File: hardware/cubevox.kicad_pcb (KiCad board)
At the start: 4 copper layers, 200 x 150 mm, 223 parts, among them J1 USB-C, J101 J_IN NCJ6FA-H, J106 DC 9V, J108 OUT 6.35mm, J117 OLED SH1106, J3 TC2030-NL SWD, K101 G6K-2F-Y DC5, K102 G6K-2F-Y DC5, Q101 MMBT3904, SW101 ST-0-102 bat toggle, SW102 ST-0-102 bat toggle, SW103 ST-0-102 bat toggle, SW104 ST-0-102 bat toggle, SW105 ST-0-102 bat toggle, SW106 ST-0-102 bat toggle, SW107 ST-0-102 bat toggle, SW108 ST-0-102 bat toggle, U1 STM32H743VIT6, U101 CD74HC4067, U103 AP63205WU-7, U104 OPA2197IDR, U105 OPA2197IDR, U106 OPA2197IDR, U3 AP63203WU-7, U4 TLV75533PDBVR, U6 PCM5102APWR, U8 PCM1808PWR, Y1 25MHz 12pF

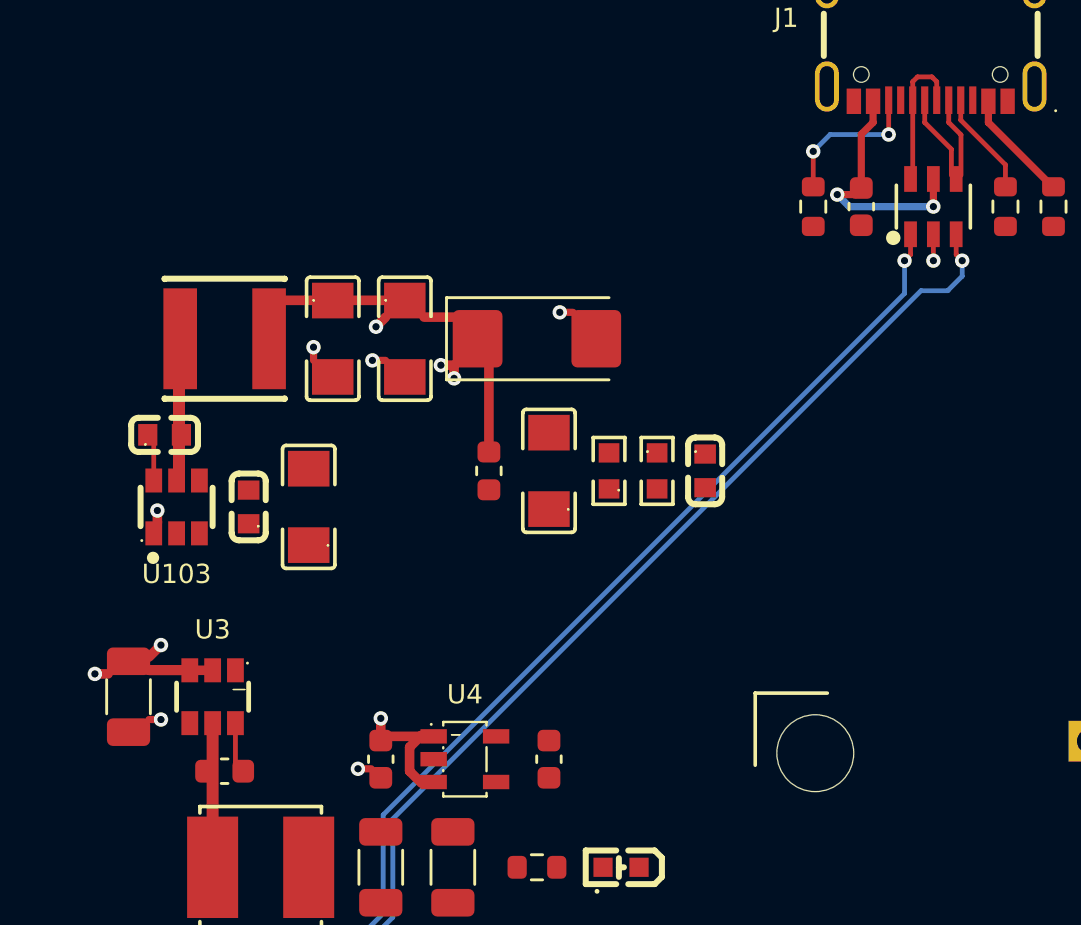
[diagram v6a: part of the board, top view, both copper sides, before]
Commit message: layout: change on /5V,/GND (ledger 0096)
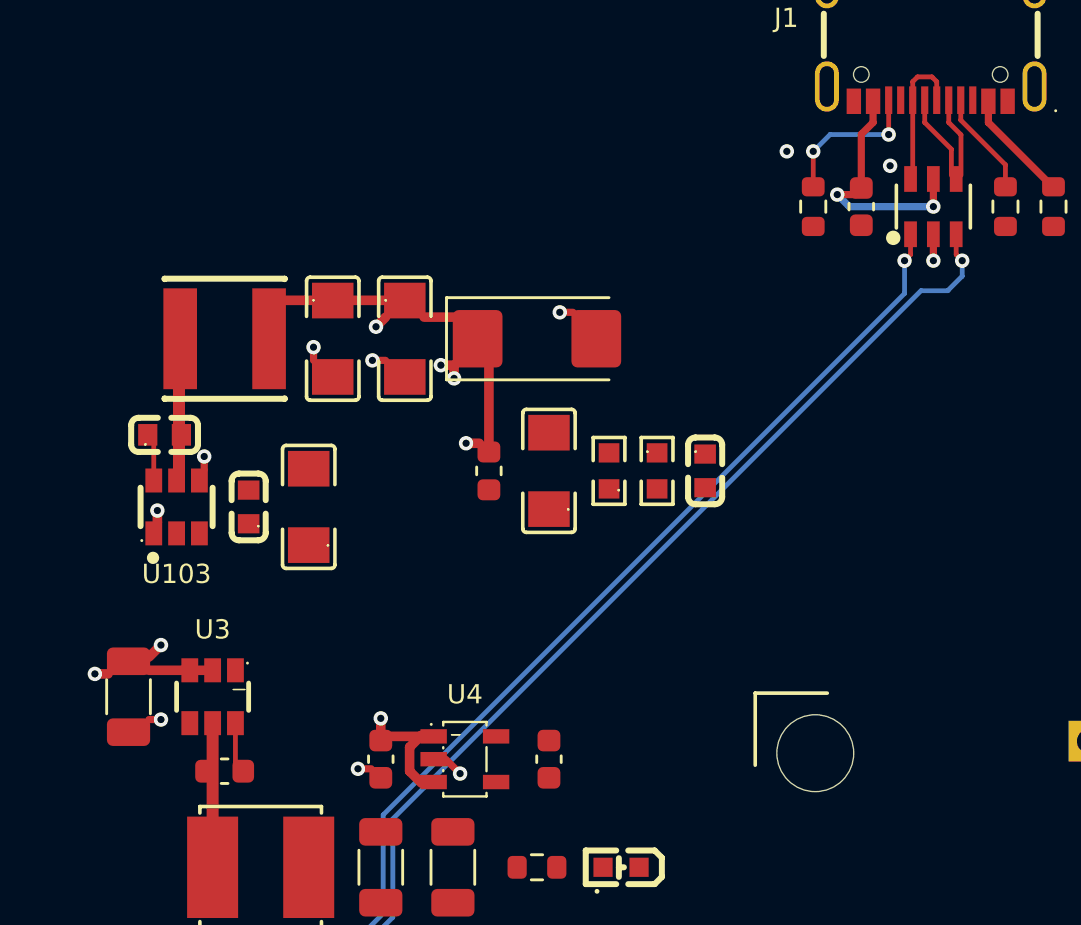
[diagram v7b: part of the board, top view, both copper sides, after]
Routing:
- net /GND: track 3.80 -> 5.20 mm, vias 7 -> 11
- net /5V: track 94.8 -> 94.0 mm, vias 8 -> 9
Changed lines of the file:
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@@
 	)
 	(segment
-		(start 125.5 41.65)
-		(end 125.5 42.75)
-		(width 0.2)
+		(start 105.2 63.5)
+		(end 105.8 64.099999)
+		(width 0.3)
 		(layer "F.Cu")
 		(net "/GND")
@@
 	)
 	(segment
+		(start 125.5 41.65)
+		(end 125.5 42.75)
+		(width 0.3)
+		(layer "F.Cu")
+		(net "/GND")
+	)
+	(segment
+		(start 95.15 51.45)
+		(end 95.15 50.9)
+		(width 0.3)
+		(layer "F.Cu")
+		(net "/GND")
+	)
+	(segment
 		(start 92.85 61.85)
 		(end 93.35 61.85)
@@
 	)
 	(via
+		(at 119.4 38.2)
+		(size 0.6)
+		(drill 0.3)
+		(layers "F.Cu" "B.Cu")
+		(net "/GND")
+	)
+	(via
+		(at 105.8 64.099999)
+		(size 0.6)
+		(drill 0.3)
+		(layers "F.Cu" "B.Cu")
+		(net "/GND")
+	)
+	(via
 		(at 109.95 44.9)
 		(size 0.6)
@@
 	)
 	(via
+		(at 123.7 38.8)
+		(size 0.6)
+		(drill 0.3)
+		(layers "F.Cu" "B.Cu")
+		(net "/GND")
+	)
+	(via
 		(at 101.55 63.9)
 		(size 0.6)
@@
 	(via
 		(at 125.5 42.75)
+		(size 0.6)
+		(drill 0.3)
+		(layers "F.Cu" "B.Cu")
+		(net "/GND")
+	)
+	(via
+		(at 95.15 50.9)
 		(size 0.6)
 		(drill 0.3)
@@
 	)
 	(segment
-		(start 92.85 59.8)
-		(end 95.2 59.8)
-		(width 0.4)
-		(layer "F.Cu")
-		(net "/5V")
-	)
-	(segment
 		(start 104.2 62.5)
 		(end 103.7 63)
@@
 	)
 	(segment
+		(start 94.25 59.8)
+		(end 95.2 59.8)
+		(width 0.4)
+		(layer "F.Cu")
+		(net "/5V")
+	)
+	(segment
 		(start 105.55 47.1)
 		(end 105 47.1)
@@
 	)
 	(segment
+		(start 106.6 50.35)
+		(end 106.05 50.35)
+		(width 0.4)
+		(layer "F.Cu")
+		(net "/5V")
+	)
+	(segment
 		(start 93.35 58.75)
 		(end 92.85 59.25)
@@
 		(size 0.6)
 		(drill 0.3)
+		(layers "F.Cu" "B.Cu")
+		(net "/5V")
+	)
+	(via
+		(at 106.05 50.35)
+		(size 0.6)
+		(drill 0.3)

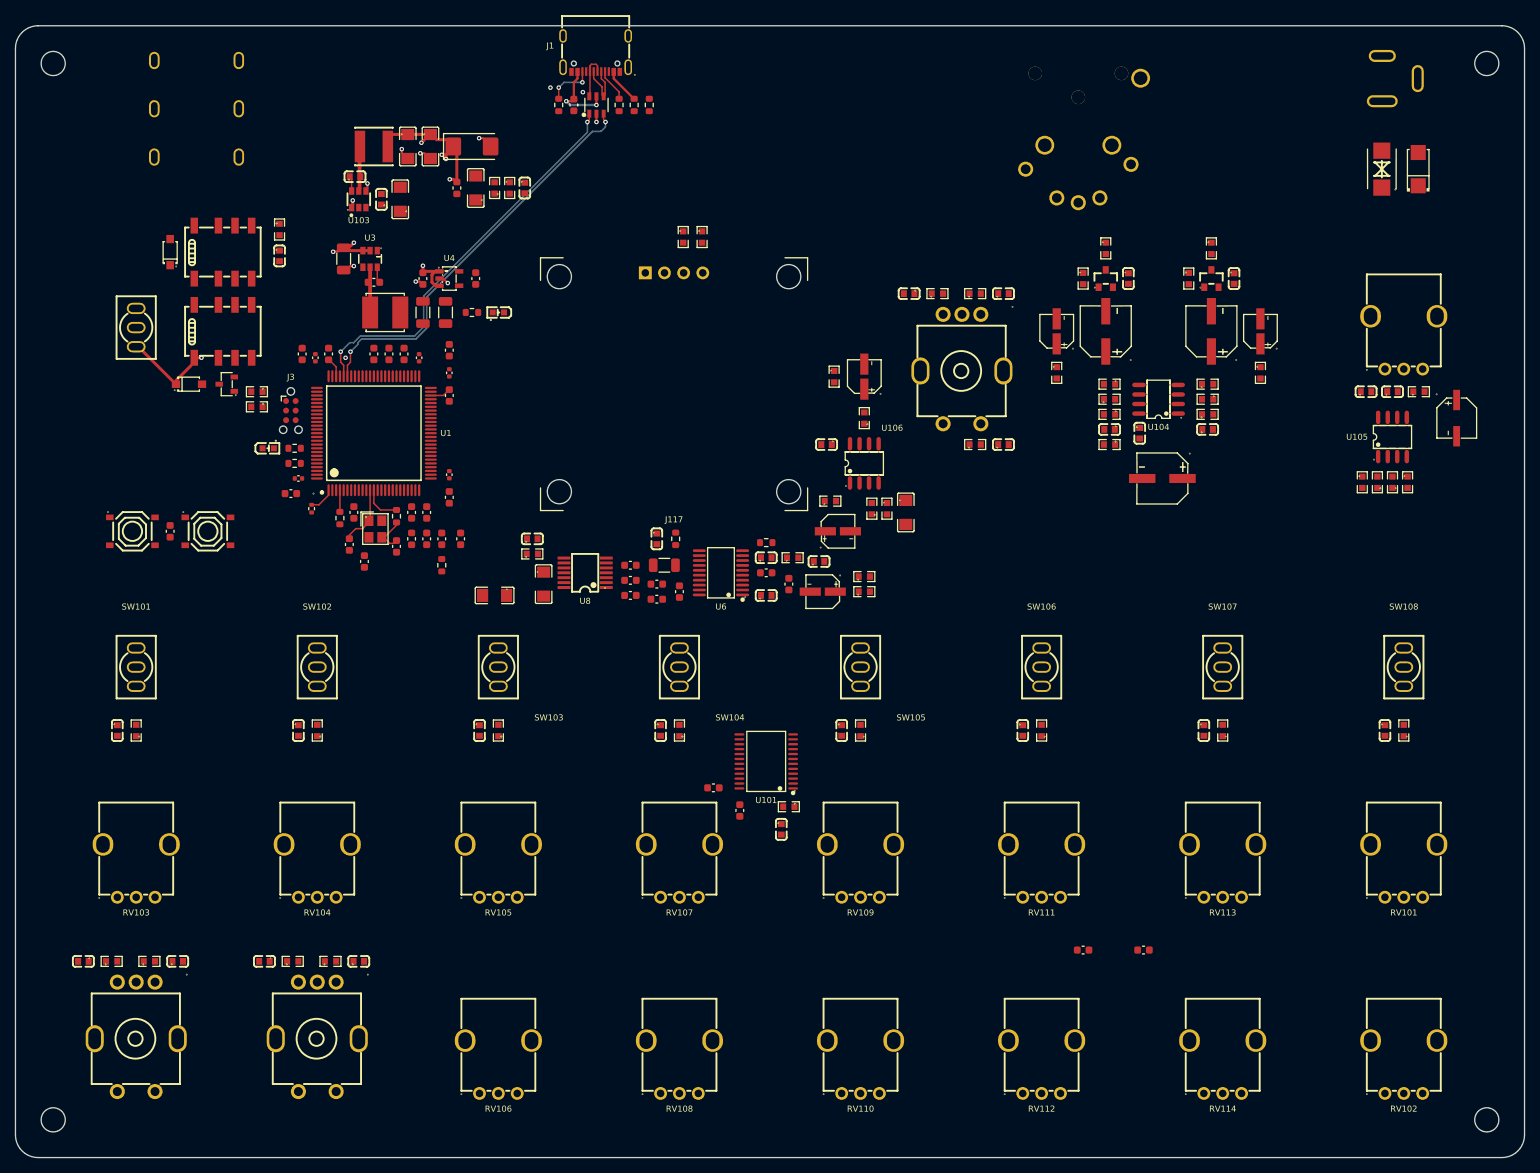
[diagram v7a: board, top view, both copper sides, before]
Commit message: layout: change on /3V3,/GND (ledger 0097)
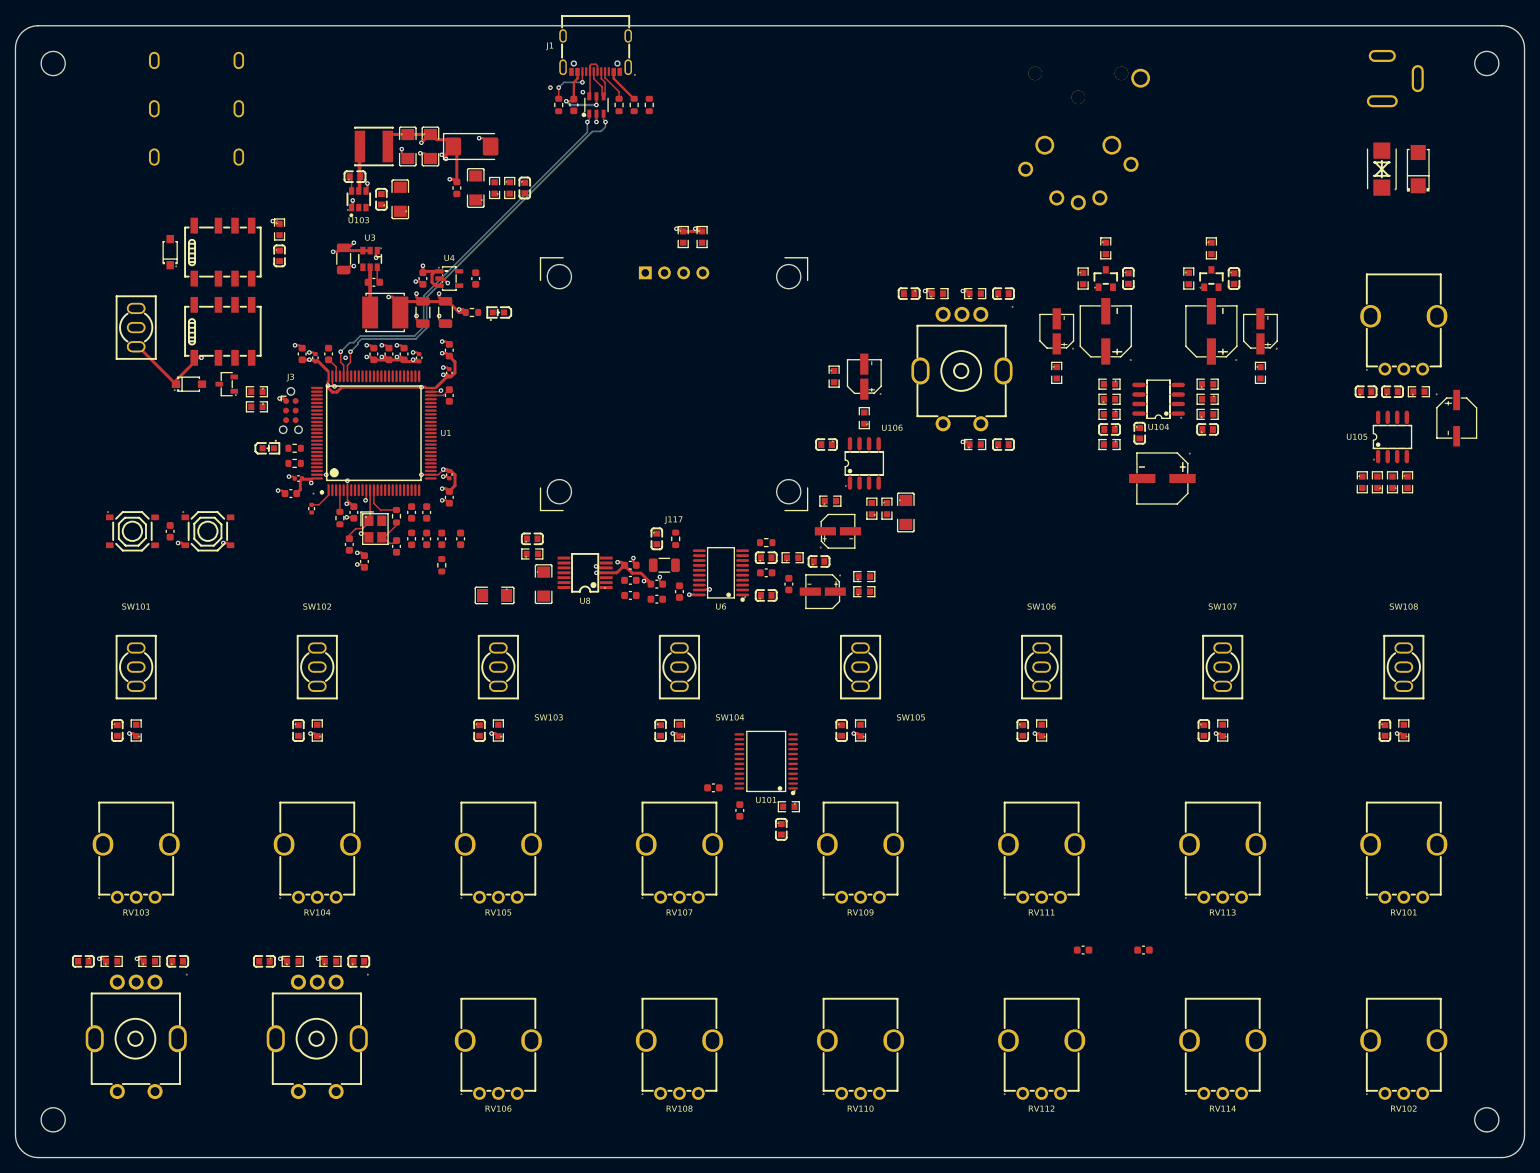
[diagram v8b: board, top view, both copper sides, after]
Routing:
- net /3V3: track 0.00 -> 610.6 mm, vias 0 -> 47
- net /GND: track 5.20 -> 18.5 mm, vias 11 -> 35
